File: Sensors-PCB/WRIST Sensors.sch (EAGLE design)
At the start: 22 parts, among them U1 VL6180X, U10 VL6180X, U2 VL6180X, U3 VL6180X, U4 VL6180X, U5 VL6180X, U6 VL6180X, U7 VL6180X, U8 VL6180X, U9 VL6180X

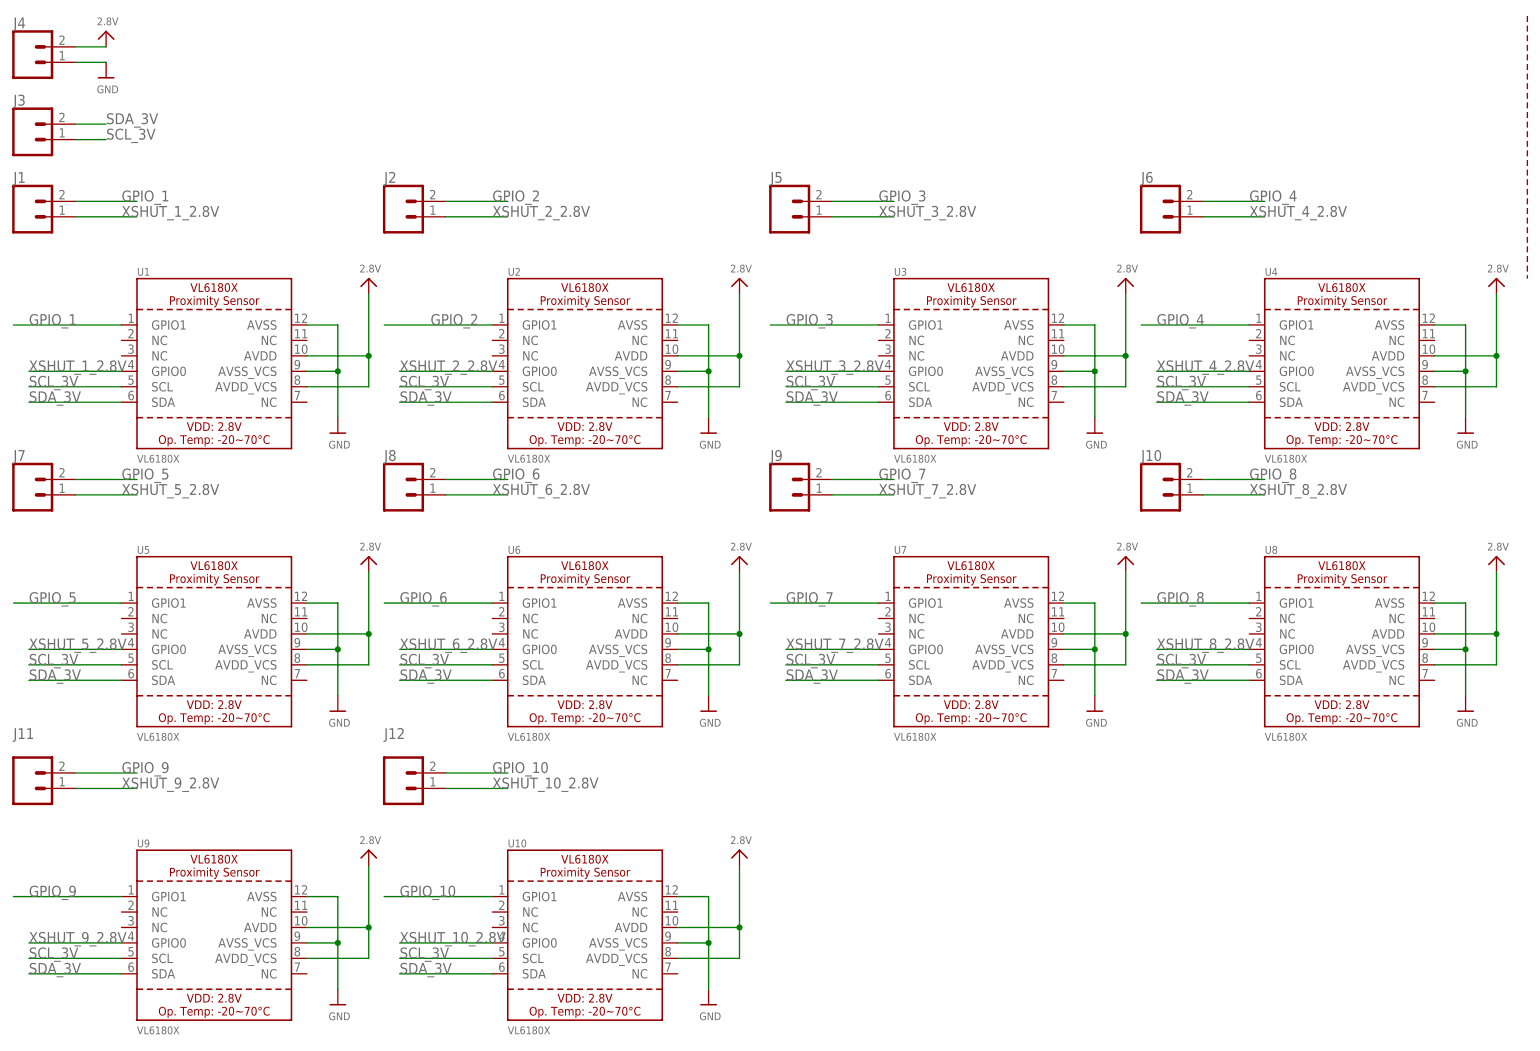
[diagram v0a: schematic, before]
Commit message: add 20 pin header and rename board
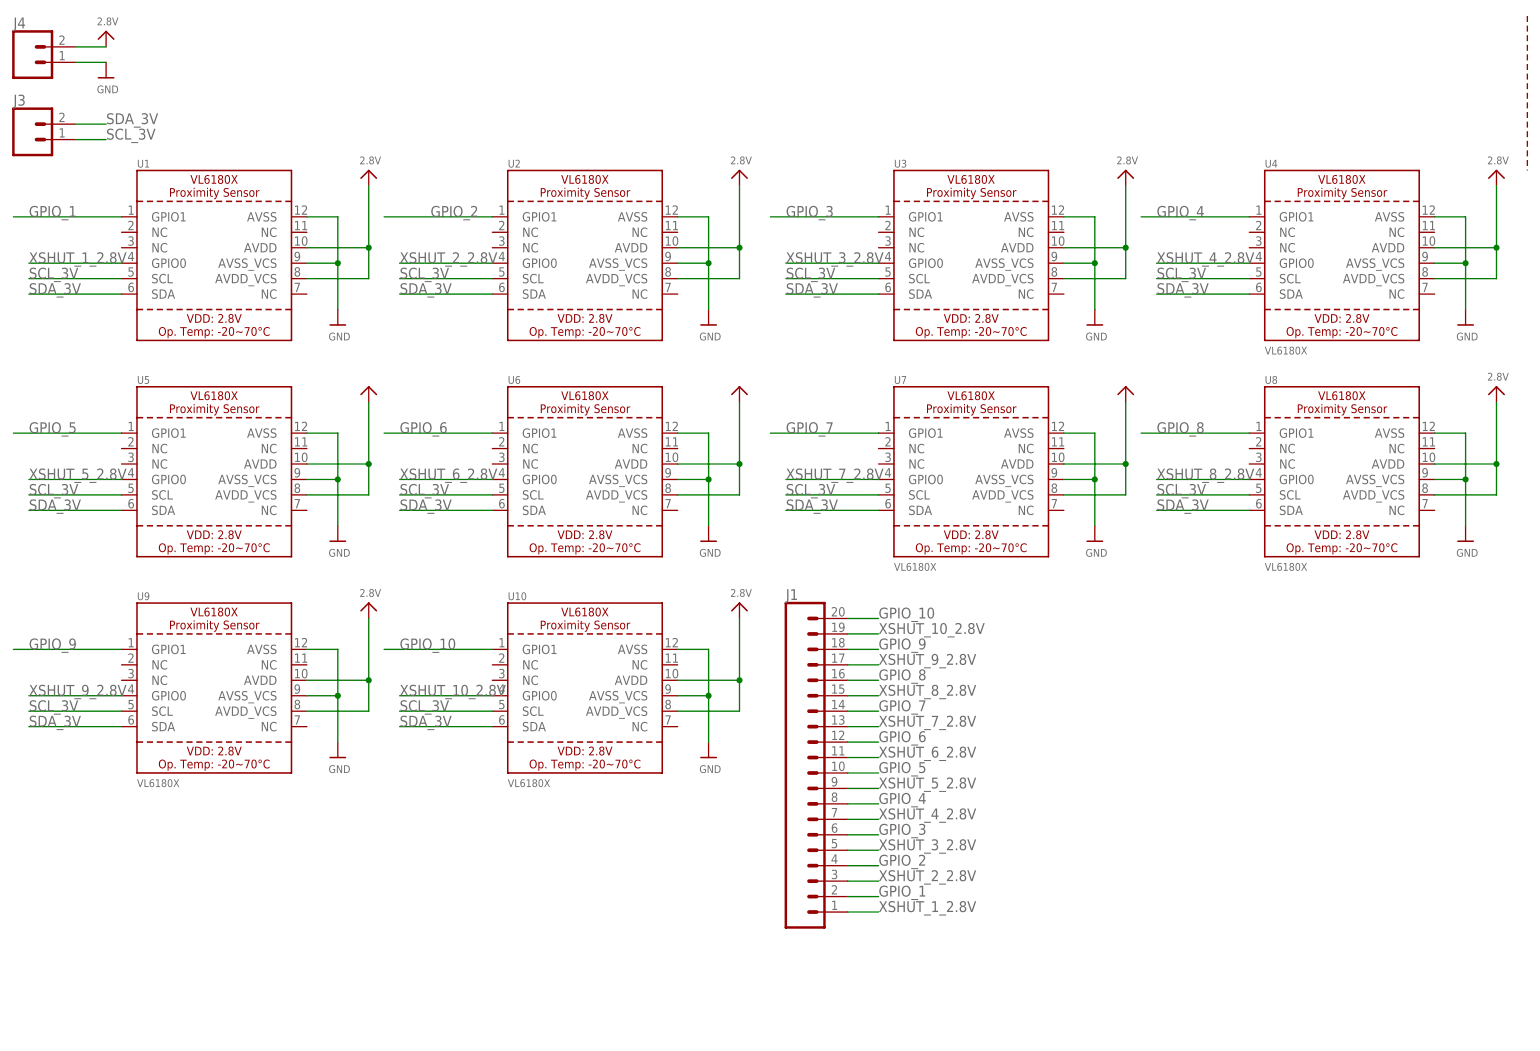
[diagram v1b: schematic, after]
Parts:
- removed J10, J11, J12, J2, J5, J6, J7, J8, J9: (no value), SparkFun-Connectors:CONN_021X02_NO_SILK
- J1: device SparkFun-Connectors:CONN_021X02_NO_SILK -> SparkFun-Connectors:CONN_20NOSILK
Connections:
- net GPIO_10: now also J1.20; no longer J12.2
- net GPIO_2: now also J1.4; no longer J2.2
- net GPIO_3: now also J1.6; no longer J5.2
- net GPIO_4: now also J1.8; no longer J6.2
- net GPIO_5: now also J1.10; no longer J7.2
- net GPIO_6: now also J1.12; no longer J8.2
- net GPIO_7: now also J1.14; no longer J9.2
- net GPIO_8: now also J1.16; no longer J10.2
- net GPIO_9: now also J1.18; no longer J11.2
- net XSHUT_10_2.8V: now also J1.19; no longer J12.1
- net XSHUT_2_2.8V: now also J1.3; no longer J2.1
- net XSHUT_3_2.8V: now also J1.5; no longer J5.1
- net XSHUT_4_2.8V: now also J1.7; no longer J6.1
- net XSHUT_5_2.8V: now also J1.9; no longer J7.1
- net XSHUT_6_2.8V: now also J1.11; no longer J8.1
- net XSHUT_7_2.8V: now also J1.13; no longer J9.1
- net XSHUT_8_2.8V: now also J1.15; no longer J10.1
- net XSHUT_9_2.8V: now also J1.17; no longer J11.1
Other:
- moved on the sheet: U1, U10, U2, U3, U4, U5, U6, U7, U8, U9

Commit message: progress
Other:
- moved on the sheet: J1, J3, J4, U1, U10, U2, U3, U4, U5, U6, U7, U8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
